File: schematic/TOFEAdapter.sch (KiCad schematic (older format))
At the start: 2 parts, among them U1 TOFE-8X, U2 TOFE-8X

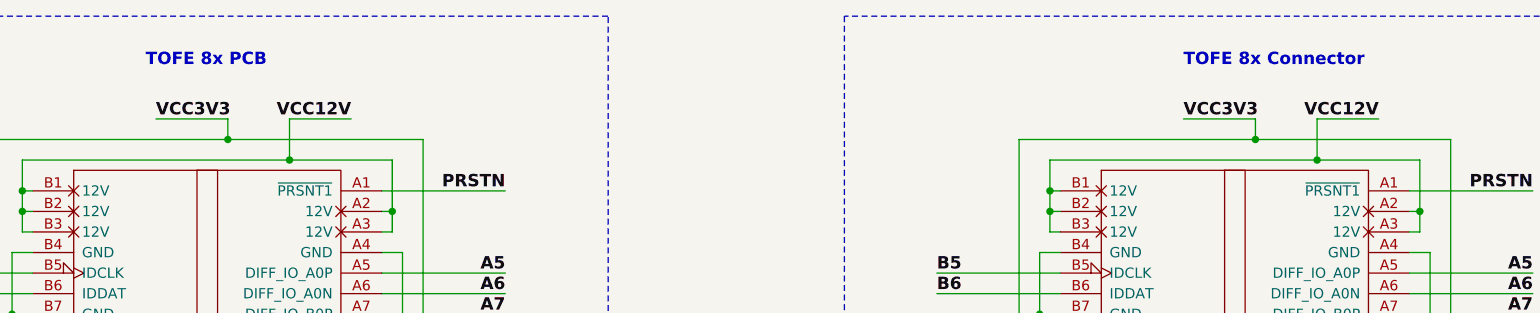
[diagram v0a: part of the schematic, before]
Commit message: Removing text.
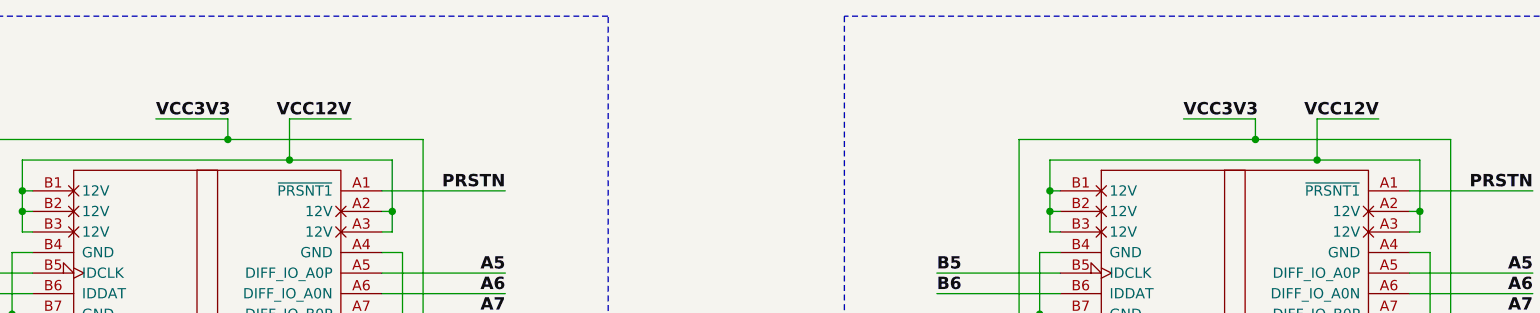
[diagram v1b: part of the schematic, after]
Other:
- note removed: "TOFE 8x Connector"
- note removed: "TOFE 8x PCB"
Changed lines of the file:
@@
 Text Label 5450 2200 2    60   ~ 12
 VCC12V
-Text Notes 4450 1950 0    60   ~ 12
-TOFE 8x PCB
 Text Label 3300 4050 0    60   ~ 12
 B14
@@
 Text Label 9500 2200 0    60   ~ 12
 VCC3V3
-Text Notes 9500 1950 0    60   ~ 12
-TOFE 8x Connector
 Text Label 8300 4050 0    60   ~ 12
 B14

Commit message: Updating the .net file.
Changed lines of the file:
@@
 	3900 2850 3800 2850
 Wire Wire Line
-	3800 2850 3800 3150
-Wire Wire Line
-	3800 3150 3800 3950
-Wire Wire Line
-	3800 3950 3800 4250
-Wire Wire Line
-	3800 4250 3800 4450
-Wire Wire Line
-	3800 4450 3800 4850
-Wire Wire Line
-	3800 4850 3800 4950
-Wire Wire Line
-	3800 4950 3800 5250
-Wire Wire Line
-	3800 5250 3800 5350
-Wire Wire Line
-	3800 5350 3800 5650
-Wire Wire Line
-	3800 5650 3800 5950
-Wire Wire Line
-	3800 5950 3800 6350
-Wire Wire Line
-	3800 6350 3800 6450
-Wire Wire Line
-	3800 6450 3800 6750
-Wire Wire Line
-	3800 6750 3800 6850
-Wire Wire Line
-	3800 6850 3800 7150
-Wire Wire Line
-	3800 7150 3800 7250
-Wire Wire Line
-	3800 7250 3800 7550
-Wire Wire Line
-	3800 7550 3800 7750
-Wire Wire Line
-	3800 7750 3800 8300
+	3800 2850 3800 8300
 Wire Wire Line
 	3800 3150 3900 3150
@@
 	5600 2850 5700 2850
 Wire Wire Line
-	5700 2850 5700 3850
-Wire Wire Line
-	5700 3850 5700 4150
-Wire Wire Line
-	5700 4150 5700 4450
-Wire Wire Line
-	5700 4450 5700 4750
-Wire Wire Line
-	5700 4750 5700 5050
-Wire Wire Line
-	5700 5050 5700 5150
-Wire Wire Line
-	5700 5150 5700 5450
-Wire Wire Line
-	5700 5450 5700 5550
-Wire Wire Line
-	5700 5550 5700 5850
-Wire Wire Line
-	5700 5850 5700 6250
-Wire Wire Line
-	5700 6250 5700 6550
-Wire Wire Line
-	5700 6550 5700 6650
-Wire Wire Line
-	5700 6650 5700 6950
-Wire Wire Line
-	5700 6950 5700 7050
-Wire Wire Line
-	5700 7050 5700 7350
-Wire Wire Line
-	5700 7350 5700 7450
-Wire Wire Line
-	5700 7450 5700 7750
-Wire Wire Line
-	5700 7750 5700 8300
+	5700 8300 5700 2850
 Wire Wire Line
 	5700 4150 5600 4150
@@
 Connection ~ 5700 7450
 Wire Wire Line
-	5700 8300 4700 8300
-Wire Wire Line
-	4700 8300 3800 8300
+	3800 8300 5700 8300
 Connection ~ 3800 7750
 Connection ~ 5700 7750
@@
 	3700 3450 3900 3450
 Wire Wire Line
-	3700 2300 3700 3250
-Wire Wire Line
-	3700 3250 3700 3450
+	3700 2300 3700 3450
 Wire Wire Line
 	3700 3250 3900 3250
@@
 	5600 3350 5800 3350
 Wire Wire Line
-	5800 2300 5800 3350
-Wire Wire Line
-	5800 3350 5800 3450
+	5800 2300 5800 3450
 Wire Wire Line
 	5800 3450 5600 3450
 Wire Wire Line
-	3700 2300 4850 2300
-Wire Wire Line
-	4850 2300 5800 2300
+	3700 2300 5800 2300
 Connection ~ 5800 3350
 Connection ~ 3700 3250
@@
 	3850 2750 3900 2750
 Wire Wire Line
-	3850 2400 3850 2550
-Wire Wire Line
-	3850 2550 3850 2650
-Wire Wire Line
-	3850 2650 3850 2750
+	3850 2400 3850 2750
 Wire Wire Line
 	3850 2650 3900 2650
@@
 	5650 2750 5600 2750
 Wire Wire Line
-	5650 2400 5650 2650
-Wire Wire Line
-	5650 2650 5650 2750
+	5650 2400 5650 2750
 Wire Wire Line
 	5650 2650 5600 2650
 Wire Wire Line
-	3850 2400 5150 2400
-Wire Wire Line
-	5150 2400 5650 2400
+	3850 2400 5650 2400
 Connection ~ 5650 2650
 Connection ~ 3850 2550
@@
 	8900 2850 8800 2850
 Wire Wire Line
-	8800 2850 8800 3150
-Wire Wire Line
-	8800 3150 8800 3950
-Wire Wire Line
-	8800 3950 8800 4250
-Wire Wire Line
-	8800 4250 8800 4450
-Wire Wire Line
-	8800 4450 8800 4850
-Wire Wire Line
-	8800 4850 8800 4950
-Wire Wire Line
-	8800 4950 8800 5250
-Wire Wire Line
-	8800 5250 8800 5350
-Wire Wire Line
-	8800 5350 8800 5650
-Wire Wire Line
-	8800 5650 8800 5950
-Wire Wire Line
-	8800 5950 8800 6350
-Wire Wire Line
-	8800 6350 8800 6450
-Wire Wire Line
-	8800 6450 8800 6750
-Wire Wire Line
-	8800 6750 8800 6850
-Wire Wire Line
-	8800 6850 8800 7150
-Wire Wire Line
-	8800 7150 8800 7250
-Wire Wire Line
-	8800 7250 8800 7550
-Wire Wire Line
-	8800 7550 8800 7750
-Wire Wire Line
-	8800 7750 8800 8300
+	8800 2850 8800 8300
 Wire Wire Line
 	8800 3150 8900 3150
@@
 	10600 2850 10700 2850
 Wire Wire Line
-	10700 2850 10700 3850
-Wire Wire Line
-	10700 3850 10700 4150
-Wire Wire Line
-	10700 4150 10700 4450
-Wire Wire Line
-	10700 4450 10700 4750
-Wire Wire Line
-	10700 4750 10700 5050
-Wire Wire Line
-	10700 5050 10700 5150
-Wire Wire Line
-	10700 5150 10700 5450
-Wire Wire Line
-	10700 5450 10700 5550
-Wire Wire Line
-	10700 5550 10700 5850
-Wire Wire Line
-	10700 5850 10700 6250
-Wire Wire Line
-	10700 6250 10700 6550
-Wire Wire Line
-	10700 6550 10700 6650
-Wire Wire Line
-	10700 6650 10700 6950
-Wire Wire Line
-	10700 6950 10700 7050
-Wire Wire Line
-	10700 7050 10700 7350
-Wire Wire Line
-	10700 7350 10700 7450
-Wire Wire Line
-	10700 7450 10700 7750
-Wire Wire Line
-	10700 7750 10700 8300
+	10700 8300 10700 2850
 Wire Wire Line
 	10700 4150 10600 4150
@@
 Connection ~ 10700 7450
 Wire Wire Line
-	10700 8300 9700 8300
-Wire Wire Line
-	9700 8300 8800 8300
+	8800 8300 10700 8300
 Connection ~ 8800 7750
 Connection ~ 10700 7750
@@
 	8700 3450 8900 3450
 Wire Wire Line
-	8700 2300 8700 3250
-Wire Wire Line
-	8700 3250 8700 3450
+	8700 2300 8700 3450
 Wire Wire Line
 	8700 3250 8900 3250
@@
 	10600 3350 10800 3350
 Wire Wire Line
-	10800 2300 10800 3350
-Wire Wire Line
-	10800 3350 10800 3450
+	10800 2300 10800 3450
 Wire Wire Line
 	10800 3450 10600 3450
 Wire Wire Line
-	8700 2300 9850 2300
-Wire Wire Line
-	9850 2300 10800 2300
+	8700 2300 10800 2300
 Connection ~ 10800 3350
 Connection ~ 8700 3250
@@
 	8850 2750 8900 2750
 Wire Wire Line
-	8850 2400 8850 2550
-Wire Wire Line
-	8850 2550 8850 2650
-Wire Wire Line
-	8850 2650 8850 2750
+	8850 2400 8850 2750
 Wire Wire Line
 	8850 2650 8900 2650
@@
 	10650 2750 10600 2750
 Wire Wire Line
-	10650 2400 10650 2650
-Wire Wire Line
-	10650 2650 10650 2750
+	10650 2400 10650 2750
 Wire Wire Line
 	10650 2650 10600 2650
 Wire Wire Line
-	8850 2400 10150 2400
-Wire Wire Line
-	10150 2400 10650 2400
+	8850 2400 10650 2400
 Connection ~ 10650 2650
 Connection ~ 8850 2550
